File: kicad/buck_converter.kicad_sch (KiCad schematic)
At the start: 46 parts, among them J5 SolderPad, J6 SolderPad, Q2 CSD19537Q3, Q3 BSZ096N10LS5, U2 LM5146

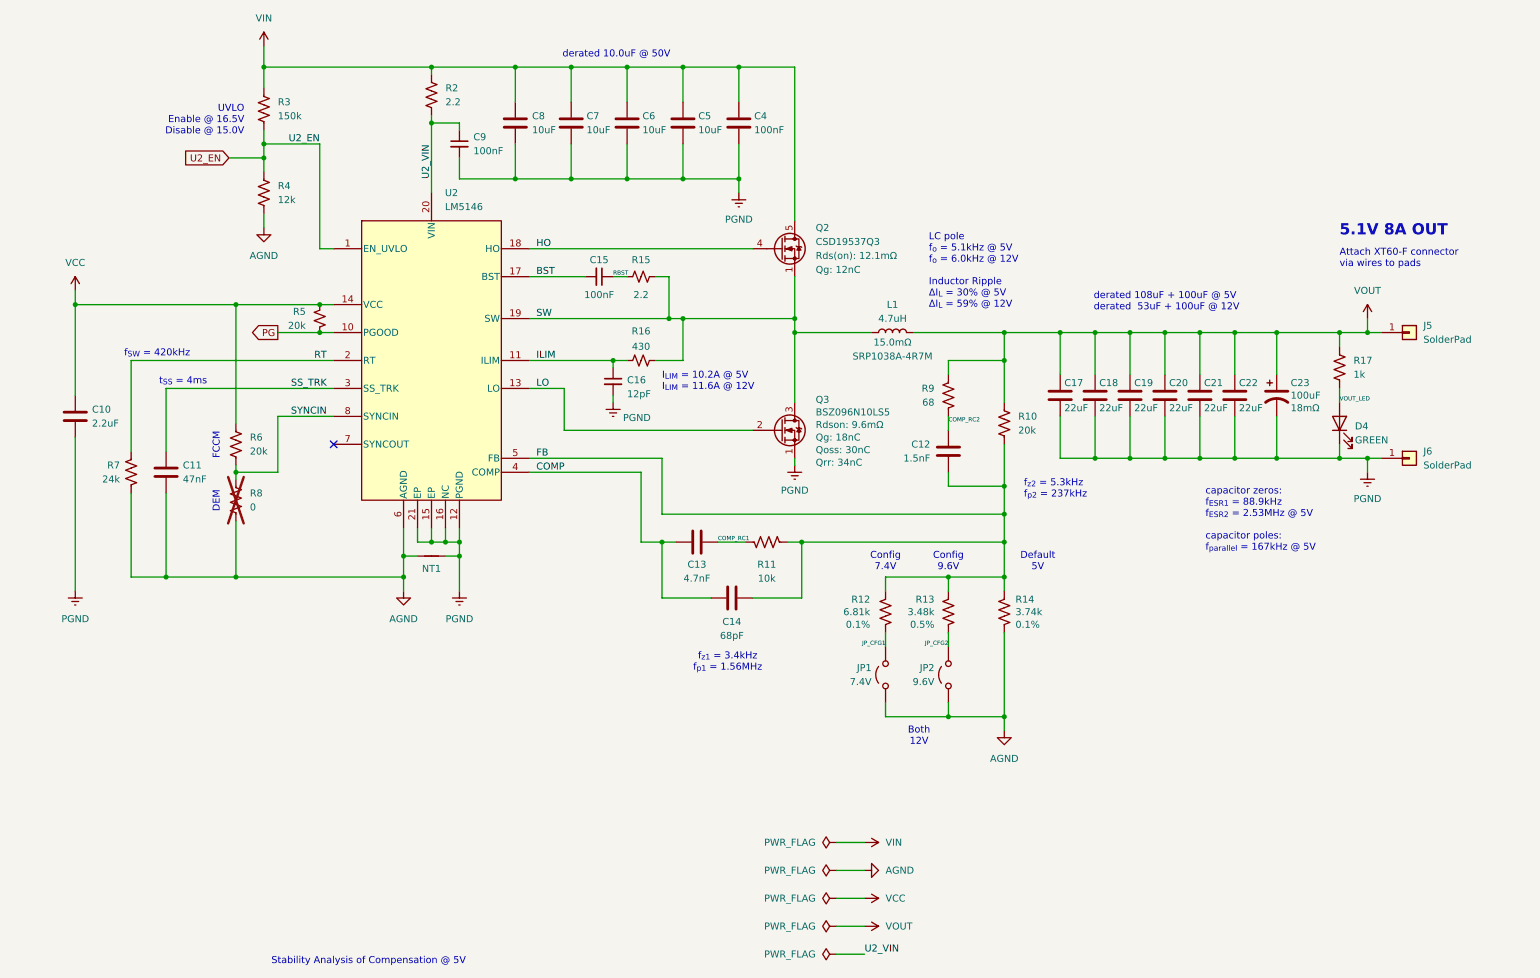
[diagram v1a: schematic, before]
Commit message: Created redesign for revD to reduce thermal stress
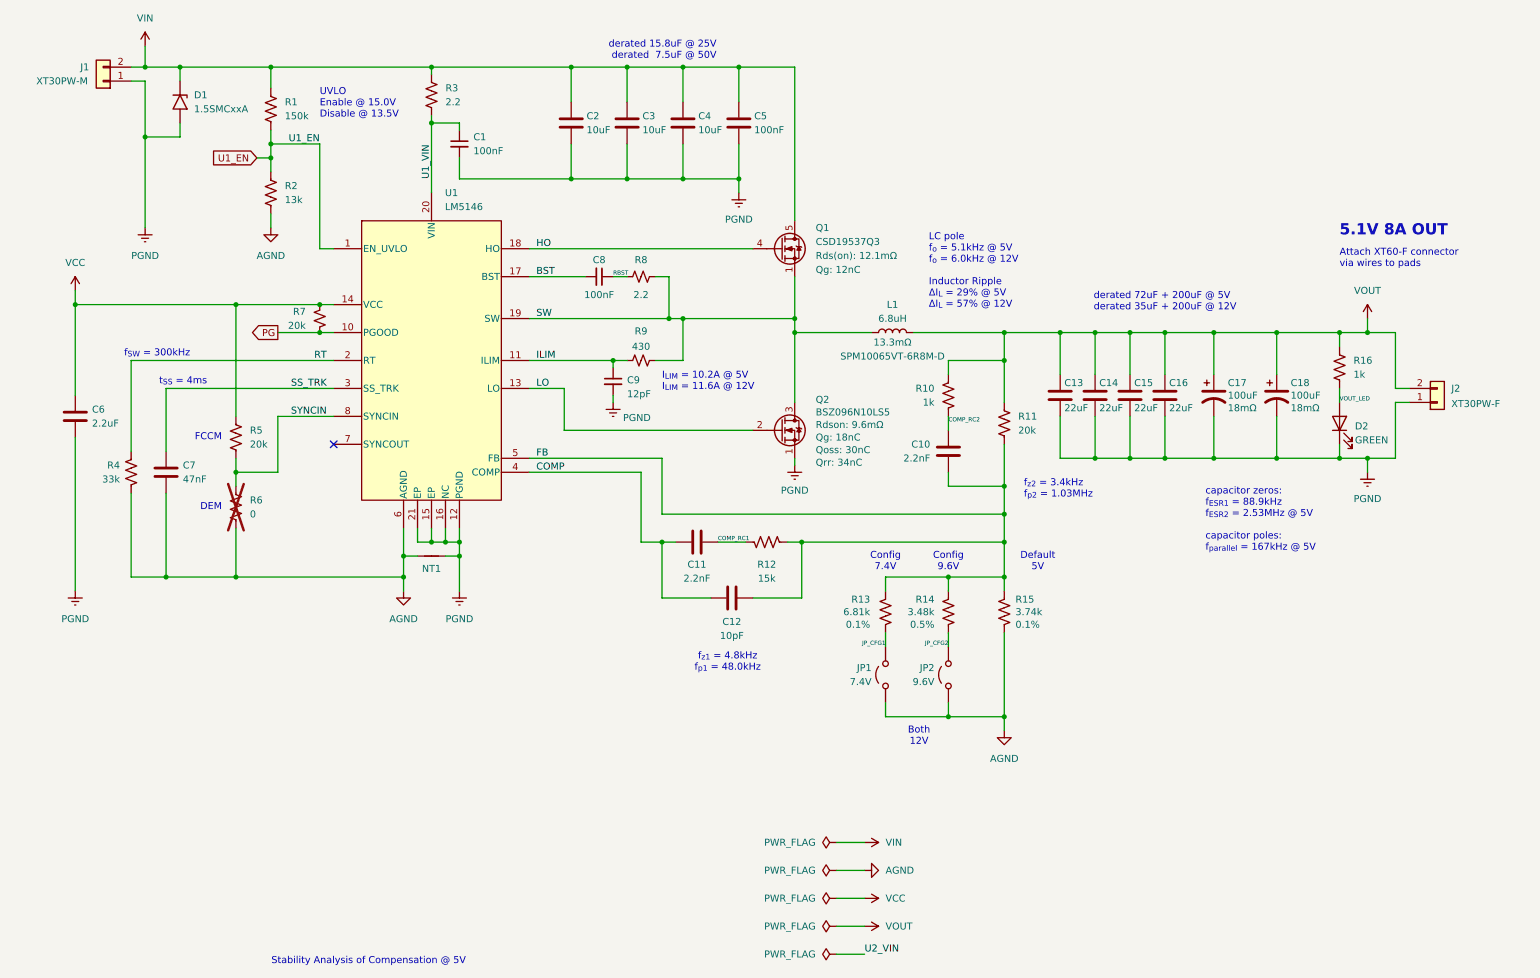
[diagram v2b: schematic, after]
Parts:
- removed C13: 4.7nF, Capacitor_SMD:C_0603_1608Metric, symbol Device:C
- removed C21, C22: 22uF, Capacitor_SMD:C_1210_3225Metric, symbol Device:C
- removed C8: 10uF, Capacitor_SMD:C_1210_3225Metric, symbol Device:C
- removed J5, J6: SolderPad, Connector_Wire:SolderWirePad_1x01_SMD_3x6mm, symbol Connector_Generic:Conn_01x01
- added C11: 2.2nF, Capacitor_SMD:C_0603_1608Metric, symbol Device:C
- added C17: 100uF, Capacitor_Tantalum_SMD:CP_EIA-7343-20_Kemet-V_HandSolder, symbol Device:C_Polarized_US
- added D1: 1.5SMCxxA, Diode_SMD:D_SMC, symbol Diode:1.5SMCxxA
- added J1: XT30PW-M, Connector_AMASS:AMASS_XT30PW-M_1x02_P2.50mm_Horizontal, symbol Connector_Generic:Conn_01x02
- added J2: XT30PW-F, Connector_AMASS:AMASS_XT30PW-F_1x02_P2.50mm_Horizontal, symbol Connector_Generic:Conn_01x02
- C10: renamed from C12; value 1.5nF -> 2.2nF; LCSC PN C1595 -> C1604; Part Number 0603B152K500NT -> 0603B222K500NT; Part Type Preferred Extended -> Basic
- C12: renamed from C14; value 68pF -> 10pF; LCSC PN C28262 -> C1634; Part Number CL10C680JB8NNNC -> CL10C100JB8NNNC; Part Type Preferred Extended -> Basic
- L1: value 4.7uH -> 6.8uH; footprint Inductor_SMD:L_Bourns_SRP1038C_10.0x10.0mm -> Inductor_SMD:L_Vishay_IHLP-4040; ESR 15.0mΩ -> 13.3mΩ; LCSC ALT1 C6949325 -> (none); LCSC PN C2041319 -> C2047831; Manufacturer Bourns -> TDK; PART ALT1 PA4342.472NLT -> (none); Part Number SRP1038A-4R7M -> SPM10065VT-6R8M-D
- Q2: renamed from Q3; footprint Package_SON_JJ:Infineon_PG-TSDSON-8-26_3.3x3.3mm_P0.65mm -> Package_SON_JJ:Infineon_PG-TSDSON-8-26_3.3x3.3mm_P0.65mm_ThermalVias-D0.3mm
- R10: renamed from R9; value 68 -> 1k; LCSC PN C27592 -> C21190; Part Number 0603WAF680JT5E -> 0603WAF1001T5E; Part Type Preferred Extended -> Basic
- R12: renamed from R11; value 10k -> 15k; LCSC PN C25804 -> C22809; Part Number 0603WAF1002T5E -> 0603WAF1502T5E
- R2: renamed from R4; value 12k -> 13k; LCSC PN C22790 -> C22797; Part Number 0603WAF1202T5E -> 0603WAF1302T5E
- R4: renamed from R7; value 24k -> 33k; LCSC PN C23352 -> C4216; Part Number 0603WAF2402T5E -> 0603WAF3302T5E
- renumbered C9 to C1, C17 to C13, C18 to C14, C19 to C15, C20 to C16, C23 to C18, C7 to C2, C6 to C3, C5 to C4, C4 to C5, C10 to C6, C11 to C7, C15 to C8, C16 to C9, D4 to D2, Q2 to Q1, R3 to R1, R10 to R11, R12 to R13, R13 to R14, R14 to R15, R17 to R16, R2 to R3, R6 to R5, R8 to R6, R5 to R7, R15 to R8, R16 to R9, U2 to U1
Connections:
- net COMP: now also C11.1
- net COMP_RC1: now also C11.2
- net PGND: now also C17.2, D1.2 (A2), J1.1 (Pin_1), J2.1 (Pin_1)
- net U2_VIN: no longer C1.1, R3.2, U1.20 (VIN)
- net VIN: now also D1.1 (A1), J1.2 (Pin_2)
- net VOUT: now also C17.1, J2.2 (Pin_2)
- net U2_EN renamed U1_EN
- new net U1_VIN: C1.1, R3.2, U1.20 (VIN)
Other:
- note added: "LC pole f_{o} = 5.1kHz @ 5V f_{o} = 6.0kHz @ 12V Inductor Ripple ΔI_{L} = 29% @ 5V ΔI_{L} = 57% @ 12V"
- note added: "UVLO Enable @ 15.0V Disable @ 13.5V"
- note added: "derated 15.8uF @ 25V derated 7.5uF @ 50V"
- note added: "derated 72uF + 200uF @ 5V derated 35uF + 200uF @ 12V"
- note added: "f_{SW} = 300kHz"
- note added: "f_{z1} = 4.8kHz f_{p1} = 48.0kHz"
- note added: "f_{z2} = 3.4kHz f_{p2} = 1.03MHz"
- note removed: "LC pole f_{o} = 5.1kHz @ 5V f_{o} = 6.0kHz @ 12V Inductor Ripple ΔI_{L} = 30% @ 5V ΔI_{L} = 59% @ 12V"
- note removed: "UVLO Enable @ 16.5V Disable @ 15.0V"
- note removed: "derated 10.0uF @ 50V"
- note removed: "derated 108uF + 100uF @ 5V derated 53uF + 100uF @ 12V"
- note removed: "f_{SW} = 420kHz"
- note removed: "f_{z1} = 3.4kHz f_{p1} = 1.56MHz"
- note removed: "f_{z2} = 5.3kHz f_{p2} = 237kHz"
- moved on the sheet: R1, R2, R5, R6

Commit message: FET Optimizations
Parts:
- removed C17: 100uF, Capacitor_Tantalum_SMD:CP_EIA-7343-20_Kemet-V_HandSolder, symbol Device:C_Polarized_US
- removed C3: 10uF, Capacitor_SMD:C_1210_3225Metric, symbol Device:C
- removed Q1: CSD19537Q3, Package_SON_JJ:Texas_DQG0008A_3.3x3.3mm_P0.65mm_ThermalVias-D0.3mm, symbol Transistor_FET:CSD19537Q3
- removed R4: 33k, Resistor_SMD:R_0603_1608Metric, symbol Device:R_US
- added C1: 100uF, Connector_Wire:SolderWire-0.5sqmm_1x02_P4.6mm_D0.9mm_OD2.1mm, symbol Device:C_Polarized_US
- added C10, C11, C9: 100nF, Capacitor_SMD:C_0603_1608Metric, symbol Device:C
- added C23: 22uF, Capacitor_SMD:C_1206_3216Metric, symbol Device:C
- added C6, C7, C8: 4.7uF, Capacitor_SMD:C_1206_3216Metric, symbol Device:C
- added Q1: BSZ146N10LS5ATMA1, Package_SON_JJ:Infineon_PG-TSDSON-8-26_3.3x3.3mm_P0.65mm_ThermalVias-D0.3mm, symbol Julian_Symbols:BSZ096N10LS5
- added R5: 24k, Resistor_SMD:R_0603_1608Metric, symbol Device:R_US
- C19: renamed from C13; footprint Capacitor_SMD:C_1210_3225Metric -> Capacitor_SMD:C_1206_3216Metric; LCSC PN C309062 -> C5272872; Manufacturer Panasonic -> Murata Electronics; Part Number CL32B226KAJNNNE -> GRM31CC71E226ME15L
- C20: renamed from C14; footprint Capacitor_SMD:C_1210_3225Metric -> Capacitor_SMD:C_1206_3216Metric; LCSC PN C309062 -> C5272872; Manufacturer Panasonic -> Murata Electronics; Part Number CL32B226KAJNNNE -> GRM31CC71E226ME15L
- C21: renamed from C15; footprint Capacitor_SMD:C_1210_3225Metric -> Capacitor_SMD:C_1206_3216Metric; LCSC PN C309062 -> C5272872; Manufacturer Panasonic -> Murata Electronics; Part Number CL32B226KAJNNNE -> GRM31CC71E226ME15L
- C22: renamed from C16; footprint Capacitor_SMD:C_1210_3225Metric -> Capacitor_SMD:C_1206_3216Metric; LCSC PN C309062 -> C5272872; Manufacturer Panasonic -> Murata Electronics; Part Number CL32B226KAJNNNE -> GRM31CC71E226ME15L
- C3: renamed from C2; value 10uF -> 4.7uF; footprint Capacitor_SMD:C_1210_3225Metric -> Capacitor_SMD:C_1206_3216Metric; LCSC PN C576517 -> C3864744; Part Number GRM32EC72A106KE05L -> GRJ31CZ72A475KE01L
- C4: value 10uF -> 4.7uF; footprint Capacitor_SMD:C_1210_3225Metric -> Capacitor_SMD:C_1206_3216Metric; LCSC PN C576517 -> C3864744; Part Number GRM32EC72A106KE05L -> GRJ31CZ72A475KE01L
- C5: value 100nF -> 4.7uF; footprint Capacitor_SMD:C_0603_1608Metric -> Capacitor_SMD:C_1206_3216Metric; ESR (none) -> 2mΩ; LCSC PN C113803 -> C3864744; Manufacturer YAGEO -> Murata Electronics; Part Number CC0603KRX7R0BB104 -> GRJ31CZ72A475KE01L
- D1: value 1.5SMCxxA -> SMBJ64A; footprint Diode_SMD:D_SMC -> Diode_SMD:D_SMB
- J1: value XT30PW-M -> XT30U-M; footprint Connector_AMASS:AMASS_XT30PW-M_1x02_P2.50mm_Horizontal -> Connector_AMASS:AMASS_XT30U-M_1x02_P5.0mm_Vertical; LCSC PN (none) -> C99101; Manufacturer (none) -> Changzhou Amass Elec; Part Number (none) -> XT30U-M; Part Type (none) -> Extended
- J2: value XT30PW-F -> XT30U-F; footprint Connector_AMASS:AMASS_XT30PW-F_1x02_P2.50mm_Horizontal -> Connector_AMASS:AMASS_XT30U-F_1x02_P5.0mm_Vertical; LCSC PN (none) -> C99102; Manufacturer (none) -> Changzhou Amass Elec; Part Number (none) -> XT30U-F; Part Type (none) -> Extended
- L1: value 6.8uH -> 4.7uH; footprint Inductor_SMD:L_Vishay_IHLP-4040 -> Inductor_SMD:L_Bourns_SRP1038C_10.0x10.0mm; ESR 13.3mΩ -> 15.5mΩ; LCSC PN C2047831 -> C6949325; Manufacturer TDK -> Pulse Electronics; Part Number SPM10065VT-6R8M-D -> PA4342.472NLT
- Q2: value BSZ096N10LS5 -> BSZ146N10LS5ATMA1; footprint Package_SON_JJ:Infineon_PG-TSDSON-8-26_3.3x3.3mm_P0.65mm_ThermalVias-D0.3mm -> Package_SON_JJ:Infineon_PG-TSDSON-8-26_3.3x3.3mm_P0.65mm; ESR 9.6mΩ -> 14.6mΩ; LCSC ALT1 C534697 -> (none); LCSC PN C534695 -> C3289340; PART ALT1 BSZ097N10NS5 -> (none); Part Number BSZ096N10LS5 -> BSZ146N10LS5ATMA1; Qg 18nC -> 11nC; Qoss 30nC -> 20nC; Qrr 34nC -> 19nC; Rdson 9.6mΩ -> 14.6mΩ
- R10: renamed from R12; value 15k -> 6.8k; LCSC PN C22809 -> (none); Part Number 0603WAF1502T5E -> (none)
- renumbered C6 to C12, C7 to C13, C10 to C14, C11 to C15, C12 to C16, C8 to C17, C9 to C18, C1 to C2, C18 to C24, R3 to R1, R13 to R11, R14 to R12, R15 to R13, R8 to R14, R9 to R15, R1 to R2, R2 to R3, R7 to R4, R5 to R6, R6 to R7, R10 to R8, R11 to R9
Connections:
- net AGND: now also R5.2
- net HO: now also Q1.2 (G)
- net PGND: now also C1.2, C10.2, C11.2, C23.2, C6.2, C7.2, C8.2, C9.2
- net RT: now also R5.1
- net SW: now also Q1.1 (S)
- net VIN: now also C1.1, C10.1, C11.1, C6.1, C7.1, C8.1, C9.1, Q1.3 (D)
- net VOUT: now also C23.1
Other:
- note added: "CHANGE"
- note added: "derated 15.8uF @ 25V derated 7.6uF @ 50V"
- note added: "derated 75.0uF + 100uF @ 5V derated 36.3uF + 100uF @ 12V"
- note added: "f_{SW} = 420kHz"
- note removed: "Attach XT60-F connector via wires to pads"
- note removed: "derated 15.8uF @ 25V derated 7.5uF @ 50V"
- note removed: "derated 72uF + 200uF @ 5V derated 35uF + 200uF @ 12V"
- note removed: "f_{SW} = 300kHz"
- moved on the sheet: C24, C3, D1, D2, J1, J2, R16, R2, R3
